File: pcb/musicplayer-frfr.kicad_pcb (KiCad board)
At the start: 2 copper layers, 61.2 x 78.2 mm, 23 parts, among them J1 Battery, J2 AudioPlug3, J3 Display, SW1 SW_Push, SW2 SW_Push, SW3 SW_Push, SW4 RotaryEncoder_Switch, SW5 SW_SPDT, U1 XIAO-RP2350-SMD, U2 TP4056-42-ESOP8, U3 DFPLAYER_MINI

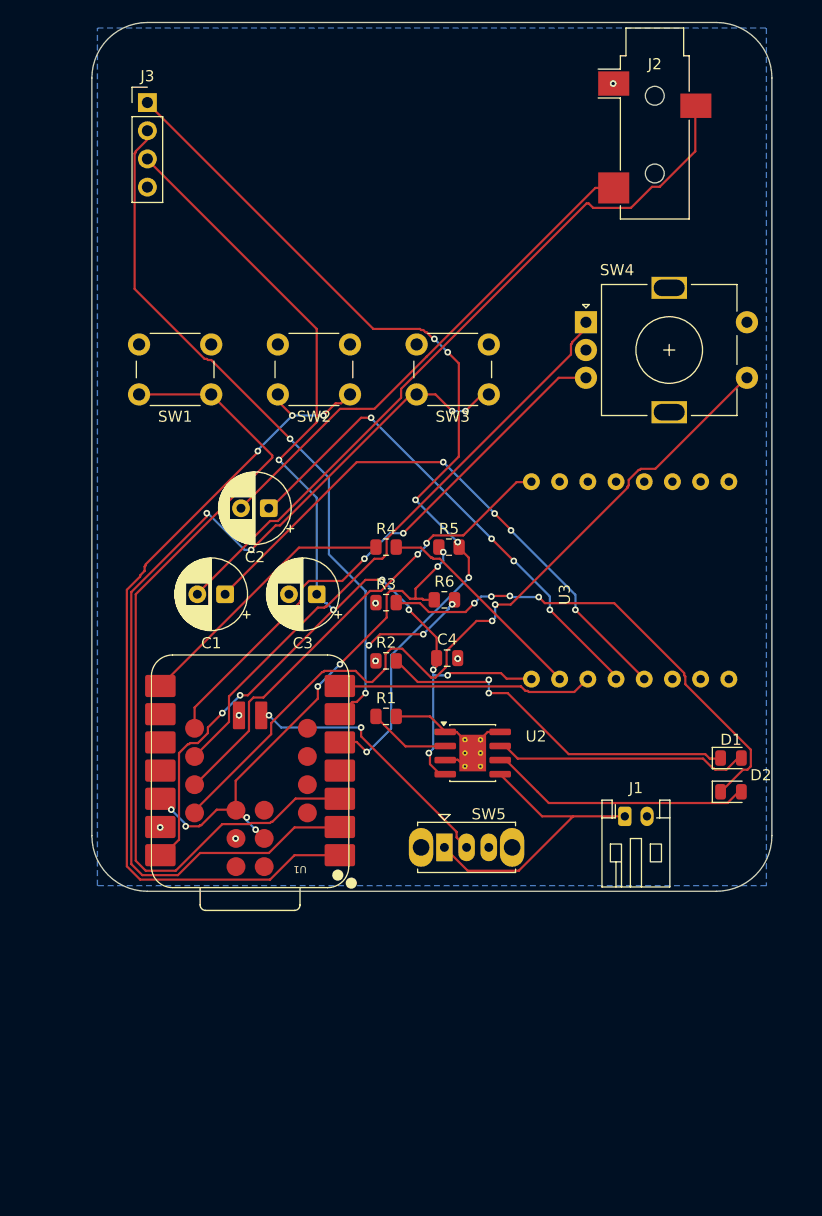
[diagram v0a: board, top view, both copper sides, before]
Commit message: fix up pcb bcuz kicad didnt place the right parts. also added fabrication files
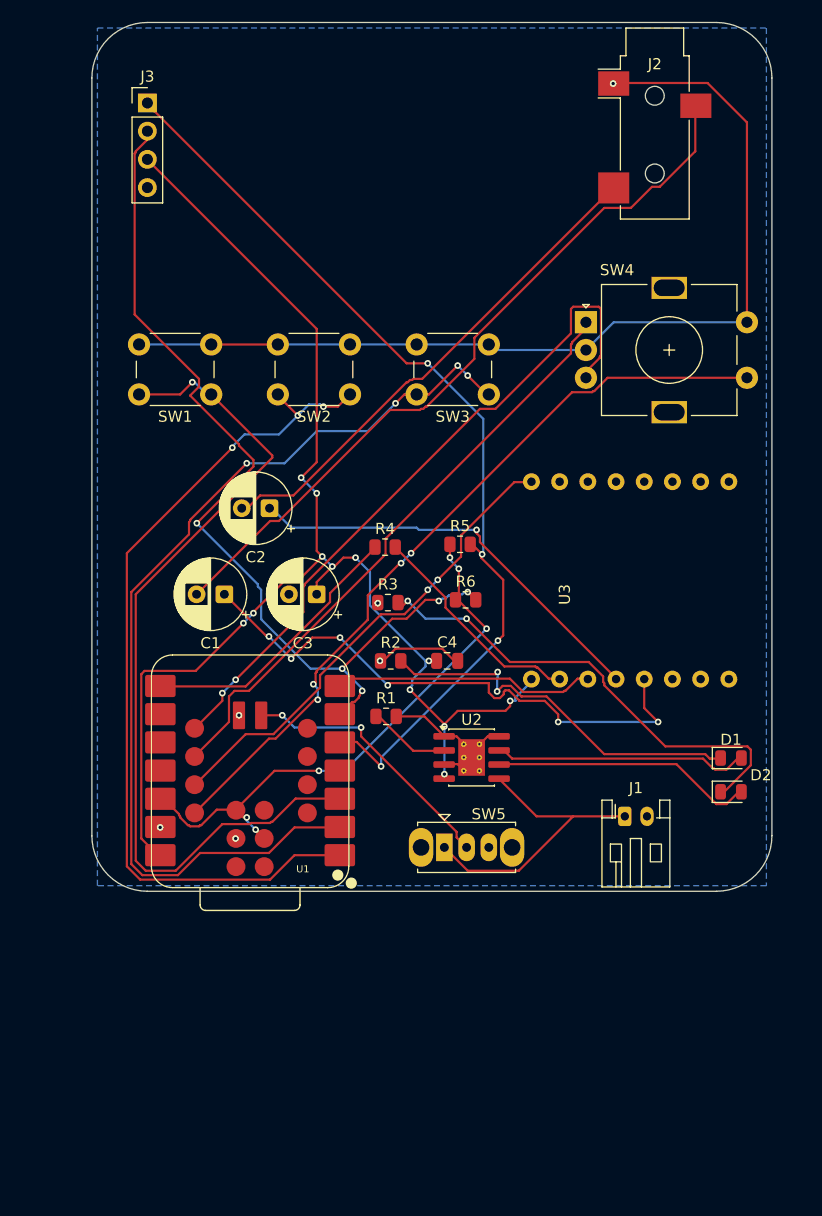
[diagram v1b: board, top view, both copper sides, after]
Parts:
- C4: value 0.1u -> 100n
- moved R6 1.91 mm to (139.9, 86.5)
- moved R5 1.03 mm to (139.4, 81.5)
- moved R2 0.41 mm to (133.2, 92.0)
- moved U2 0.41 mm to (140.4, 100.7)
- moved C4 0.25 mm to (138.2, 92.0)
- moved R3 0.16 mm to (132.9, 86.8)
- moved R4 0.09 mm to (132.7, 81.8)
- moved C2 0.07 mm to (122.2, 78.2)
- moved C1 0.07 mm to (118.2, 86.0)
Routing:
- net GND: track 11.9 -> 107.4 mm
- net /SCL: track 71.8 -> 84.3 mm
- net /ENCODER_B: track 50.2 -> 62.3 mm
- net /VBUS: track 115.5 -> 123.6 mm, vias 9 -> 12
- net Net-(U3-DAC_R): track 44.8 -> 37.9 mm, vias 4 -> 1
- net /ENCODER_SWITCH: track 72.5 -> 69.1 mm, vias 2 -> 4
- net +3V3: track 48.2 -> 51.1 mm, vias 8 -> 6
- net /SDA: track 82.8 -> 84.8 mm, vias 6 -> 4
- net /PLAY: track 75.6 -> 77.4 mm
- net /NEXT: track 89.2 -> 87.8 mm
- net Net-(D2-K): track 44.3 -> 43.3 mm, vias 4 -> 2
- net Net-(U3-RX): track 19.7 -> 20.3 mm
- net /XIAO_RX: track 23.0 -> 23.6 mm
- net /BACK: track 77.3 -> 77.8 mm, vias 0 -> 1
- net Net-(U3-DAC_L): track 51.6 -> 51.5 mm, vias 4 -> 6

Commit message: add silkscreen and hopefully prep for shipping
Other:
- board text added: "made by avy for #hardware speedrun 18-20 Aug 2026"

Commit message: layout pcb
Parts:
- removed R5, R6: 4.7k, Resistor_SMD:R_0805_2012Metric
- added C10: 1uF, Capacitor_SMD:C_0805_2012Metric_Pad1.18x1.45mm_HandSolder, F.Cu at (110.7, 107.8)
- added C11: 1uF, Capacitor_SMD:C_0805_2012Metric_Pad1.18x1.45mm_HandSolder, F.Cu at (165.5, 72.8)
- added C12: 1uF, Capacitor_SMD:C_0805_2012Metric_Pad1.18x1.45mm_HandSolder, F.Cu at (165.5, 83.8)
- added C13: 0.1u, Capacitor_SMD:C_0805_2012Metric_Pad1.18x1.45mm_HandSolder, F.Cu at (165.5, 80.8)
- added C14: 10u, Capacitor_SMD:C_0805_2012Metric_Pad1.18x1.45mm_HandSolder, F.Cu at (157.2, 113.2)
- added C15: 10u, Capacitor_SMD:C_0805_2012Metric_Pad1.18x1.45mm_HandSolder, F.Cu at (165.5, 86.8)
- added C16: 10u, Capacitor_SMD:C_0805_2012Metric_Pad1.18x1.45mm_HandSolder, F.Cu at (161.5, 113.2)
- added C17: 10u, Capacitor_SMD:C_0805_2012Metric_Pad1.18x1.45mm_HandSolder, F.Cu at (165.5, 77.8)
- added C5: 2.2uF, Capacitor_SMD:C_0805_2012Metric_Pad1.18x1.45mm_HandSolder, F.Cu at (157.0, 48.0)
- added C6: 100nF, Capacitor_SMD:C_0805_2012Metric_Pad1.18x1.45mm_HandSolder, F.Cu at (110.7, 116.9)
- added C7: 10uF, Capacitor_SMD:C_0805_2012Metric_Pad1.18x1.45mm_HandSolder, F.Cu at (166.0, 113.2)
- added C8: 2.2nF, Capacitor_SMD:C_0805_2012Metric_Pad1.18x1.45mm_HandSolder, F.Cu at (110.7, 121.5)
- added C9: 2.2nF, Capacitor_SMD:C_0805_2012Metric_Pad1.18x1.45mm_HandSolder, F.Cu at (131.5, 55.8)
- added D3: 1N4149, Diode_THT:D_DO-35_SOD27_P7.62mm_Horizontal, F.Cu at (139.0, 121.8)
- added D4: 1N4149, Diode_THT:D_DO-35_SOD27_P7.62mm_Horizontal, F.Cu at (128.0, 126.0)
- added D5: 1N4149, Diode_THT:D_DO-35_SOD27_P7.62mm_Horizontal, F.Cu at (115.4, 126.0)
- added D6: 1N4149, Diode_THT:D_DO-35_SOD27_P7.62mm_Horizontal, F.Cu at (128.0, 121.8)
- added D7: 1N4149, Diode_THT:D_DO-35_SOD27_P7.62mm_Horizontal, F.Cu at (139.0, 130.2)
- added D8: 1N4149, Diode_THT:D_DO-35_SOD27_P7.62mm_Horizontal, F.Cu at (128.0, 130.2)
- added D9: 1N4149, Diode_THT:D_DO-35_SOD27_P7.62mm_Horizontal, F.Cu at (139.0, 126.0)
- added J4: Micro_SD_Card_Det1, Connector_Card:microSD_HC_Hirose_DM3AT-SF-PEJM5, B.Cu at (160.8, 98.2)
- added R7: 4.7k, Resistor_SMD:R_0805_2012Metric_Pad1.20x1.40mm_HandSolder, F.Cu at (143.0, 56.5)
- added SW10: Next, Button_Switch_THT:SW_PUSH_6mm, F.Cu at (137.1, 110.5)
- added SW6: Select, Button_Switch_THT:SW_PUSH_6mm, F.Cu at (126.5, 102.0)
- added SW7: Right, Button_Switch_THT:SW_PUSH_6mm, F.Cu at (126.5, 110.5)
- added SW8: Prev., Button_Switch_THT:SW_PUSH_6mm, F.Cu at (137.1, 93.5)
- added SW9: Down, Button_Switch_THT:SW_PUSH_6mm, F.Cu at (137.1, 102.0)
- added TP1: USB D-, TestPoint:TestPoint_Pad_D3.0mm, F.Cu at (147.8, 86.8)
- added TP10: ESP RX, TestPoint:TestPoint_Pad_D3.0mm, F.Cu at (155.0, 79.1)
- added TP2: USB D+, TestPoint:TestPoint_Pad_D3.0mm, F.Cu at (155.0, 86.8)
- added TP3: GND, TestPoint:TestPoint_Pad_D3.0mm, F.Cu at (103.8, 71.5)
- added TP4: +5V, TestPoint:TestPoint_Pad_D3.0mm, F.Cu at (103.8, 86.0)
- added TP5: VBAT, TestPoint:TestPoint_Pad_D3.0mm, F.Cu at (104.2, 121.0)
- added TP6: +3V3, TestPoint:TestPoint_Pad_D3.0mm, F.Cu at (103.8, 78.8)
- added TP7: ESP Boot, TestPoint:TestPoint_Pad_D3.0mm, F.Cu at (148.0, 79.1)
- added TP8: ESP Enable, TestPoint:TestPoint_Pad_D3.0mm, F.Cu at (148.0, 71.5)
- added TP9: ESP TX, TestPoint:TestPoint_Pad_D3.0mm, F.Cu at (155.0, 71.5)
- added U4: ESP32-S3-WROOM-1, RF_Module:ESP32-S3-WROOM-1, B.Cu at (158.5, 53.2)
- added U5: PCF8523T, Package_SO:SOIC-8_3.9x4.9mm_P1.27mm, F.Cu at (154.0, 126.5)
- added Y1: 32.768 kHz, Crystal:Crystal_SMD_2012-2Pin_2.0x1.2mm_HandSoldering, F.Cu at (160.5, 125.8)
- C1, C2: value 100u -> 100nF; footprint Capacitor_THT:CP_Radial_D6.3mm_P2.50mm -> Capacitor_SMD:C_0805_2012Metric_Pad1.18x1.45mm_HandSolder
- C3: value 100u -> 2.2uF; footprint Capacitor_THT:CP_Radial_D6.3mm_P2.50mm -> Capacitor_SMD:C_0805_2012Metric_Pad1.18x1.45mm_HandSolder
- C4: value 100n -> 100nF; footprint Capacitor_SMD:C_0805_2012Metric -> Capacitor_SMD:C_0805_2012Metric_Pad1.18x1.45mm_HandSolder
- D1, D2: value LED -> 1N4149; footprint LED_SMD:LED_0805_2012Metric -> Diode_THT:D_DO-35_SOD27_P7.62mm_Horizontal
- J1, U1: moved to B.Cu
- J3: footprint Connector_PinHeader_2.54mm:PinHeader_1x04_P2.54mm_Vertical -> Connector_PinHeader_2.54mm:PinHeader_1x08_P2.54mm_Vertical
- R1: value 2.4K -> 470; footprint Resistor_SMD:R_0805_2012Metric -> Resistor_SMD:R_0805_2012Metric_Pad1.20x1.40mm_HandSolder
- R2: value 1K -> 470; footprint Resistor_SMD:R_0805_2012Metric -> Resistor_SMD:R_0805_2012Metric_Pad1.20x1.40mm_HandSolder
- R3: value 1K -> 10k; footprint Resistor_SMD:R_0805_2012Metric -> Resistor_SMD:R_0805_2012Metric_Pad1.20x1.40mm_HandSolder
- R4: value 1K -> 4.7k; footprint Resistor_SMD:R_0805_2012Metric -> Resistor_SMD:R_0805_2012Metric_Pad1.20x1.40mm_HandSolder
- SW1: value SW_Push -> Vol Up
- SW2: value SW_Push -> Up
- SW3: value SW_Push -> Vol Down
- SW4: value RotaryEncoder_Switch -> Left; footprint Rotary_Encoder:RotaryEncoder_Alps_EC11E-Switch_Vertical_H20mm -> Button_Switch_THT:SW_PUSH_6mm
- SW5: value SW_SPDT -> SW_BAT
- U2: value TP4056-42-ESOP8 -> TPA6130A2RTJT; footprint Package_SO:SOIC-8-1EP_3.9x4.9mm_P1.27mm_EP2.41x3.3mm_ThermalVias -> footprints:RTJ20_2P7X2P7; moved to B.Cu
- U3: value DFPLAYER_MINI -> PCM5102; footprint DFPlayer:DFPlayer_V2 -> Package_SO:TSSOP-20_4.4x6.5mm_P0.65mm; moved to B.Cu
- moved U2 64.6 mm to (107.3, 45.2), turned to 180 degrees
- moved J1 55.5 mm to (103.8, 129.2), turned to -90 degrees
- moved D2 55.1 mm to (115.4, 130.2)
- moved D1 52.7 mm to (115.4, 121.8)
- moved R1 51.8 mm to (131.5, 45.2)
- moved SW3 49.9 mm to (116.0, 110.5), turned to 0 degrees
- moved U3 49.7 mm to (107.9, 53.9), turned to 180 degrees
- moved U1 45.8 mm to (159.4, 126.1), turned to 0 degrees
- moved C1 43.2 mm to (160.7, 78.5)
- moved R2 41.5 mm to (131.5, 50.5)
- moved SW4 40.1 mm to (126.5, 93.5)
- moved J2 37.2 mm to (120.2, 49.1)
- moved SW2 36.6 mm to (116.0, 102.0), turned to 0 degrees
- moved C2 36.0 mm to (110.7, 112.3), turned to 0 degrees
- moved SW5 35.4 mm to (104.2, 98.1), turned to 90 degrees
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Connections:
- net /NEXT renamed /COL3
- C1 pad 1: Net-(U3-DAC_L) -> Net-(U3-LDOO)
- C1 pad 2: /LEFT -> GND
- C2 pad 1: Net-(U3-DAC_R) -> GND
- C2 pad 2: /RIGHT -> +3V3
- C3 pad 1: /VBUS -> Net-(U3-CAPM)
- C3 pad 2: GND -> Net-(U3-CAPP)
- C4 pad 1: /VBUS -> GND
- C4 pad 2: GND -> +3V3
- D1 pad 1: Net-(D1-K) -> /ROW1
- D1 pad 2: /CHRG -> Net-(D1-A)
- D2 pad 1: Net-(D2-K) -> /ROW1
- D2 pad 2: /STDBY -> Net-(D2-A)
- J2 pad R: /LEFT -> /Audio/HPLEFT
- J2 pad T: /RIGHT -> /Audio/HPRIGHT
- J3 pad 1: /SDA -> /DISPLAY_LIGHT
- J3 pad 2: /SCL -> /DISPLAY_RST
- J3 pad 3: /VBUS -> /DISPLAY_DC
- J3 pad 4: GND -> /DISPLAY_CS
- R1 pad 1: Net-(U2-PROG) -> Net-(C9-Pad1)
- R1 pad 2: GND -> /Audio/OUTL
- R2 pad 1: GND -> Net-(C8-Pad2)
- R2 pad 2: Net-(D1-K) -> /Audio/OUTR
- R3 pad 1: GND -> +3V3
- R3 pad 2: Net-(D2-K) -> /ESP_BOOT
- R4 pad 1: /XIAO_TX -> +3V3
- R4 pad 2: Net-(U3-RX) -> /SDA
- SW1 pad 1: /BACK -> /COL1
- SW1 pad 2: GND -> Net-(D1-A)
- SW2 pad 1: /PLAY -> /COL2
- SW2 pad 2: GND -> Net-(D2-A)
- SW3 pad 2: GND -> Net-(D3-A)
- U1 pad 1: /PLAY -> /DISPLAY_RST
- U1 pad 10: unconnected-(U1-D9-Pad10) -> /SPI_MISO
- U1 pad 11: unconnected-(U1-D10-Pad11) -> /SPI_MOSI
- U1 pad 14: /VBUS -> +5V
- U1 pad 15: /ENCODER_SWITCH -> /DISPLAY_LIGHT
- U1 pad 16: /BUSY -> unconnected-(U1-D12-Pad16)
- U1 pad 17: /ENCODER_A -> /INTA
- U1 pad 18: /ENCODER_B -> /DISPLAY_CS
- U1 pad 19: unconnected-(U1-D15-Pad19) -> /COL2
- U1 pad 20: unconnected-(U1-D16-Pad20) -> /COL1
- U1 pad 21: unconnected-(U1-D17-Pad21) -> /ROW3
- U1 pad 22: unconnected-(U1-D18-Pad22) -> /ROW2
- U1 pad 3: /BACK -> /DISPLAY_DC
- U1 pad 4: unconnected-(U1-D3-Pad4) -> /SPI_CS
- U1 pad 7: /XIAO_RX -> /ESP_ENABLE
- U1 pad 8: /XIAO_TX -> /ROW1
- U1 pad 9: unconnected-(U1-D8-Pad9) -> /SPI_SCK
- U2 pad 1: GND -> /Audio/OUTL
- U2 pad 2: Net-(U2-PROG) -> GND
- U2 pad 4: /VBUS -> /Audio/OUTR
- U2 pad 5: /VBAT -> GND
- U2 pad 6: /STDBY -> /AMP_SDN
- U2 pad 7: /CHRG -> /SCL
- U2 pad 8: GND -> /SDA
- U3 pad 1: /VBUS -> +3V3
- U3 pad 11: unconnected-(U3-IO_2-Pad11) -> GND
- U3 pad 12: unconnected-(U3-ADKEY_1-Pad12) -> GND
- U3 pad 13: unconnected-(U3-ADKEY_2-Pad13) -> /I2S_BCK
- U3 pad 14: unconnected-(U3-USB+-Pad14) -> /I2S_DIN
- U3 pad 15: unconnected-(U3-USB--Pad15) -> /I2S_LRCK
- U3 pad 16: /BUSY -> GND
- U3 pad 2: Net-(U3-RX) -> Net-(U3-CAPP)
- U3 pad 3: /XIAO_RX -> GND
- U3 pad 4: Net-(U3-DAC_R) -> Net-(U3-CAPM)
- U3 pad 5: Net-(U3-DAC_L) -> /Audio/VNEG
- U3 pad 6: unconnected-(U3-SPK_1-Pad6) -> /Audio/OUTL
- U3 pad 7: GND -> /Audio/OUTR
- U3 pad 8: unconnected-(U3-SPK_2-Pad8) -> +3V3
- U3 pad 9: unconnected-(U3-IO_1-Pad9) -> GND
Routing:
- net /VBUS: track 123.6 -> 0.00 mm, vias 12 -> 0
- net GND: track 107.4 -> 0.00 mm, vias 7 -> 0
- net /COL3: track 87.8 -> 0.00 mm, vias 4 -> 0
- net /SDA: track 84.8 -> 0.00 mm, vias 4 -> 0
- net /SCL: track 84.3 -> 0.00 mm, vias 5 -> 0
- net /BACK: track 77.8 -> 0.00 mm, vias 1 -> 0
- net /PLAY: track 77.4 -> 0.00 mm, vias 3 -> 0
- net /ENCODER_SWITCH: track 69.1 -> 0.00 mm, vias 4 -> 0
- net /LEFT: track 66.7 -> 0.00 mm
- net /ENCODER_B: track 62.3 -> 0.00 mm, vias 2 -> 0
- net /ENCODER_A: track 54.5 -> 0.00 mm
- net Net-(U3-DAC_L): track 51.5 -> 0.00 mm, vias 6 -> 0
- net +3V3: track 51.1 -> 0.00 mm, vias 6 -> 0
- net /RIGHT: track 45.4 -> 0.00 mm
- net /BUSY: track 43.4 -> 0.00 mm, vias 2 -> 0
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- removed copper zone on B.Cu, net GND
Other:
- board size 61.2 x 78.2 mm -> 70 x 100 mm
- board text removed: "DISPLAY GOES HERE"
- board text removed: "made by avy for #hardware speedrun 18-20 Aug 2026"

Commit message: route pcb
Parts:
- J4: moved to F.Cu
- moved C17 3.40 mm to (166.2, 74.4)
- moved C13 2.49 mm to (166.2, 78.4)
- moved C11 2.37 mm to (166.2, 70.5)
- moved C12 1.62 mm to (166.2, 82.3)
- moved C5 1.00 mm to (157.0, 49.0)
- moved C15 0.90 mm to (166.2, 86.2)
- moved D4 0.78 mm to (127.2, 126.0)
- moved D6 0.78 mm to (127.2, 121.8)
- moved D8 0.78 mm to (127.2, 130.2)
- moved C1 0.75 mm to (160.7, 77.8)
- turned J4 to 90 degrees
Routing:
- net +3V3: track 0.00 -> 365.7 mm, vias 0 -> 40
- net /SDA: track 0.00 -> 175.7 mm, vias 0 -> 13
- net /SCL: track 0.00 -> 164.7 mm, vias 0 -> 11
- net /ESP_ENABLE: track 0.00 -> 142.0 mm, vias 0 -> 13
- net GND: track 0.00 -> 124.3 mm, vias 0 -> 23
- net /VBAT: track 0.00 -> 122.4 mm, vias 0 -> 2
- net /SPI_SCK: track 0.00 -> 121.7 mm, vias 0 -> 8
- net /SPI_MOSI: track 0.00 -> 110.3 mm, vias 0 -> 9
- net Net-(U2-CPP): track 0.00 -> 101.6 mm, vias 0 -> 7
- net /SPI_CS: track 0.00 -> 95.2 mm, vias 0 -> 8
- net /DISPLAY_DC: track 0.00 -> 94.2 mm, vias 0 -> 7
- net Net-(U2-CPN): track 0.00 -> 90.7 mm, vias 0 -> 7
- net /DISPLAY_RST: track 0.00 -> 90.3 mm, vias 0 -> 5
- net Net-(C8-Pad2): track 0.00 -> 88.0 mm, vias 0 -> 4
- net /DAC_XSMT: track 0.00 -> 87.8 mm, vias 0 -> 2
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- added copper zone on B.Cu, net GND
